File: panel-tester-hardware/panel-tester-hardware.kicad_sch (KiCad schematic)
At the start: 13 parts, among them J1 Screw_Terminal_01x02, J2 Conn_01x02, J3 Conn_01x07, Q1 BS170, U1 INA219AxD

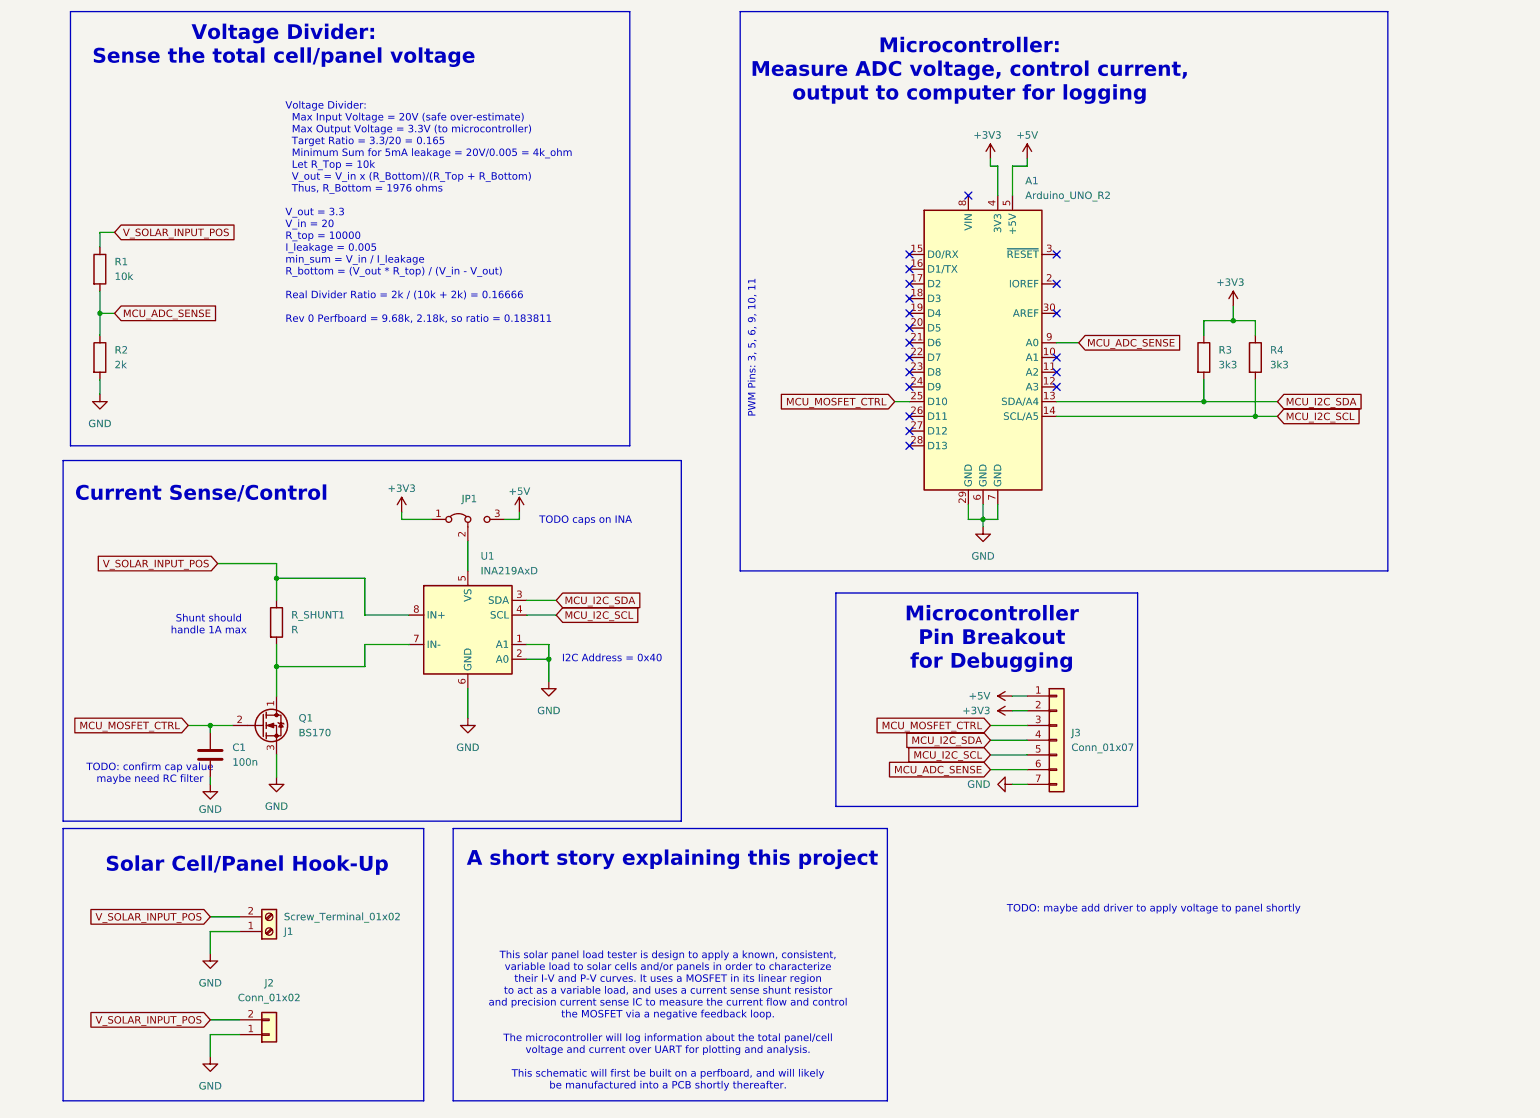
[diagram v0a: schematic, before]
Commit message: Changed Schematic Files
Modified Load Testing Schematic to use two current sensing mechanisms - (1) is the existing current sensing IC, MOSFET and shunt resistor and (2) is the new op-amp mechanism with the MOSFET and shunt resistor
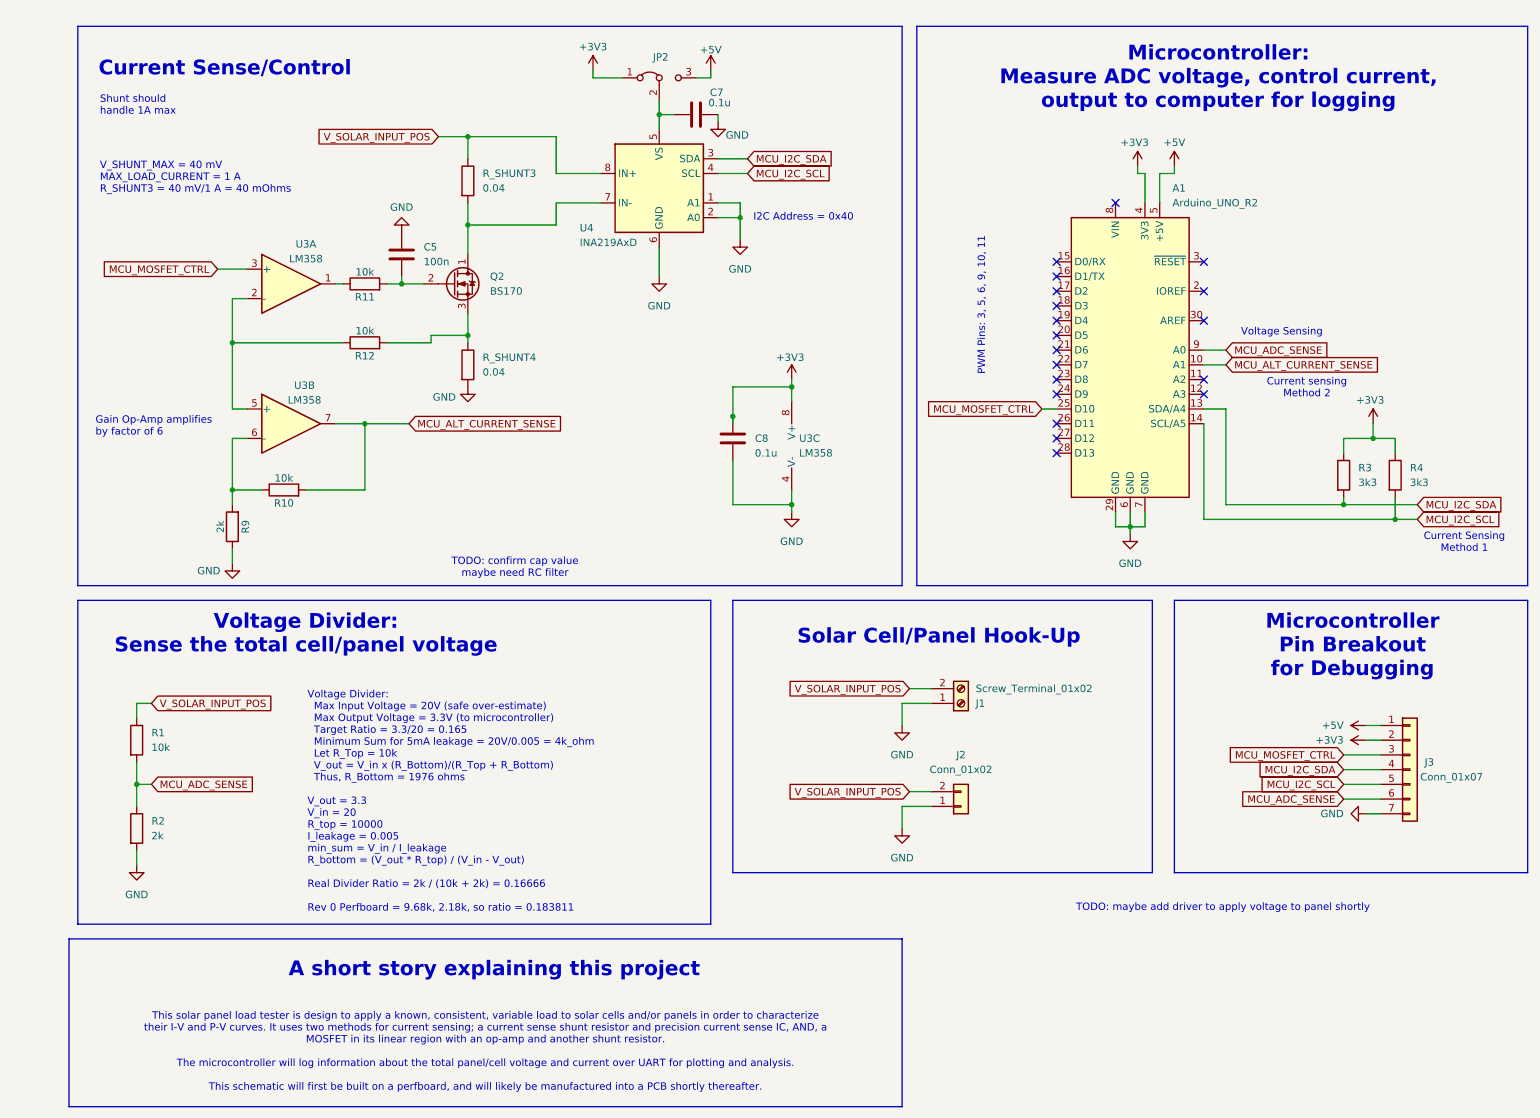
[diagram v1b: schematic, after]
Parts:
- removed C1: 100n, symbol Device:C
- removed JP1: Jumper_3_Bridged12, symbol Jumper:Jumper_3_Bridged12
- removed Q1: BS170, Package_TO_SOT_THT:TO-92_Inline, symbol Transistor_FET:BS170
- removed R_SHUNT1: R, symbol Device:R
- removed U1: INA219AxD, Package_SO:SOIC-8_3.9x4.9mm_P1.27mm, symbol Sensor_Energy:INA219AxD
- added C5: 100n, Capacitor_SMD:C_1206_3216Metric_Pad1.33x1.80mm_HandSolder, symbol Device:C
- added C7, C8: 0.1u, Capacitor_SMD:C_1206_3216Metric_Pad1.33x1.80mm_HandSolder, symbol Device:C
- added JP2: Jumper_3_Bridged12, Jumper:SolderJumper-3_P1.3mm_Open_RoundedPad1.0x1.5mm_NumberLabels, symbol Jumper:Jumper_3_Bridged12
- added Q2: BS170, Package_TO_SOT_THT:TO-92_Inline, symbol Transistor_FET:BS170
- added R10, R11, R12: 10k, Resistor_SMD:R_1206_3216Metric_Pad1.30x1.75mm_HandSolder, symbol Device:R
- added R9: 2k, Resistor_SMD:R_1206_3216Metric_Pad1.30x1.75mm_HandSolder, symbol Device:R
- added R_SHUNT3, R_SHUNT4: 0.04, Resistor_SMD:R_2512_6332Metric_Pad1.40x3.35mm_HandSolder, symbol Device:R
- added U3: LM358, Package_SO:SOIC-8_3.9x4.9mm_P1.27mm, symbol Amplifier_Operational:LM358
- added U4: INA219AxD, Package_SO:SOIC-8_3.9x4.9mm_P1.27mm, symbol Sensor_Energy:INA219AxD
- J1: footprint (none) -> TerminalBlock:TerminalBlock_bornier-2_P5.08mm
- J2: footprint (none) -> Connector_PinHeader_2.54mm:PinHeader_1x02_P2.54mm_Vertical
- J3: footprint (none) -> Connector_PinHeader_2.54mm:PinHeader_1x07_P2.54mm_Vertical
- R1, R2, R3, R4: footprint (none) -> Resistor_SMD:R_1206_3216Metric_Pad1.30x1.75mm_HandSolder
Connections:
- net +3V3: now also C8.1, JP2.1 (A), U3.8 (V+)
- net +5V: now also JP2.3 (B)
- net GND: now also C5.1, C7.2, C8.2, R9.1, R_SHUNT4.2, U3.4 (V-), U4.1 (A1), U4.2 (A0), U4.6 (GND)
- net MCU_I2C_SCL: now also U4.4 (SCL)
- net MCU_I2C_SDA: now also U4.3 (SDA)
- net MCU_MOSFET_CTRL: now also U3.3 (+)
- net V_SOLAR_INPUT_POS: now also R_SHUNT3.1, U4.8 (IN+)
- net MCU_ALT_CURRENT_SENSE: now reaches A1.10 (A1)
- net MCU_ALT_CURRENT_SENSE: now also R10.2, U3.7
- new net: R11.1, U3.1
- new net: R12.1, U3.2 (-), U3.5 (+)
- new net: C7.1, JP2.2 (C), U4.5 (VS)
- new net: C5.2, Q2.2 (G), R11.2
- new net: Q2.1 (D), R_SHUNT3.2, U4.7 (IN-)
- new net: Q2.3 (S), R12.2, R_SHUNT4.1
- new net: R10.1, R9.2, U3.6 (-)
- no-connect marks 20 -> 19
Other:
- note added: "Current Sensing Method 1"
- note added: "Current sensing Method 2"
- note added: "Gain Op-Amp amplifies by factor of 6"
- note added: "This solar panel load tester is design to apply a known, consistent, variable load to solar cells and/or panels in order to characterize their I-V and P-V curves. It uses two methods for current sensing; a current sense shunt resistor and precision current sense IC, AND, a MOSFET in its linear region with an op-amp and another shunt resistor. The microcontroller will log information about the tot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"
- note added: "V_SHUNT_MAX = 40 mV MAX_LOAD_CURRENT = 1 A R_SHUNT3 = 40 mV/1 A = 40 mOhms"
- note added: "Voltage Sensing"
- note removed: "TODO caps on INA"
- note removed: "This solar panel load tester is design to apply a known, consistent, variable load to solar cells and/or panels in order to characterize their I-V and P-V curves. It uses a MOSFET in its linear region to act as a variable load, and uses a current sense shunt resistor and precision current sense IC to measure the current flow and control the MOSFET via a negative feedback loop. The microcontroller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"
- moved on the sheet: A1, J1, J2, J3, R1, R2, R3, R4

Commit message: Did a lot of things
Created board layout and completed routing
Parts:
- Q2: footprint Package_TO_SOT_THT:TO-92_Inline -> Package_TO_SOT_THT:TO-220-3_Vertical
- U3: footprint Package_SO:SOIC-8_3.9x4.9mm_P1.27mm -> Package_DIP:DIP-8_W7.62mm_LongPads
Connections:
- net +3V3: now also J3.1 (Pin_1); no longer J3.2 (Pin_2)
- net +5V: now also J3.2 (Pin_2); no longer J3.1 (Pin_1)
- net MCU_ADC_SENSE: now also A1.10 (A1), J3.3 (Pin_3); no longer A1.9 (A0), J3.6 (Pin_6)
- net MCU_ALT_CURRENT_SENSE: now also A1.9 (A0); no longer A1.10 (A1)
- net MCU_I2C_SCL: now also J3.4 (Pin_4); no longer J3.5 (Pin_5)
- net MCU_I2C_SDA: now also J3.5 (Pin_5); no longer J3.4 (Pin_4)
- net MCU_MOSFET_CTRL: now also J3.6 (Pin_6); no longer J3.3 (Pin_3)

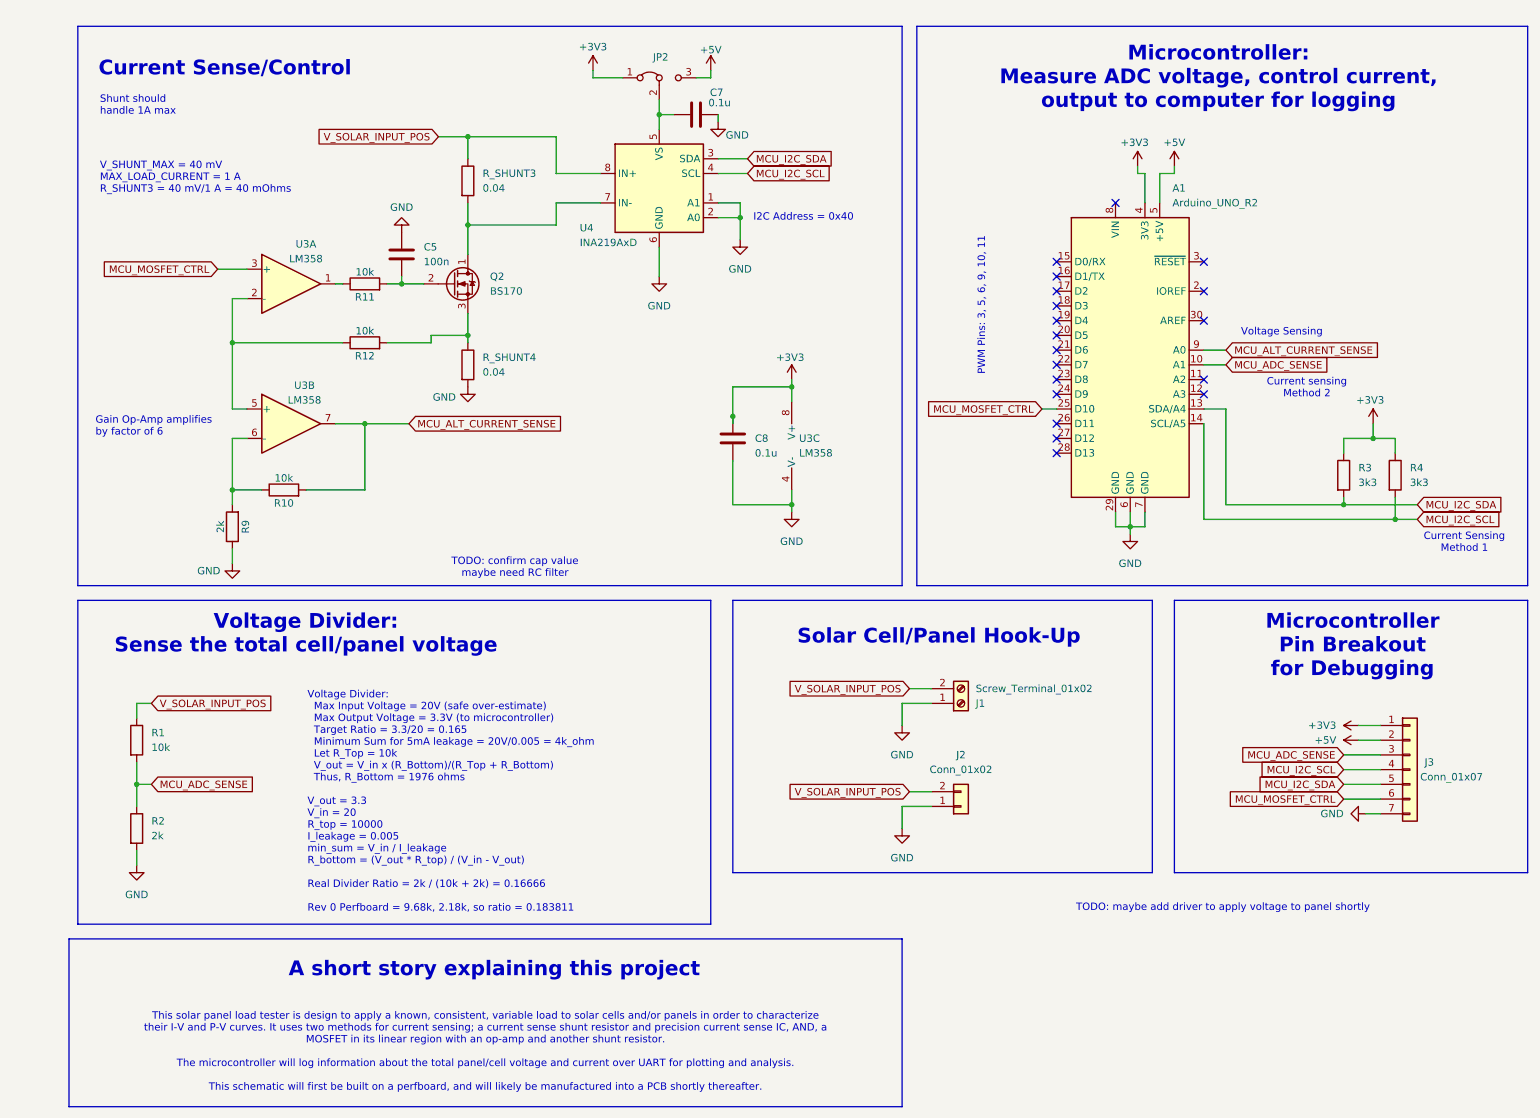
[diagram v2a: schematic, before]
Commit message: Updated schematic with DAC
Added MCP4921 for analog signal creation from Arduino PWM into the input of the Op-Amp.
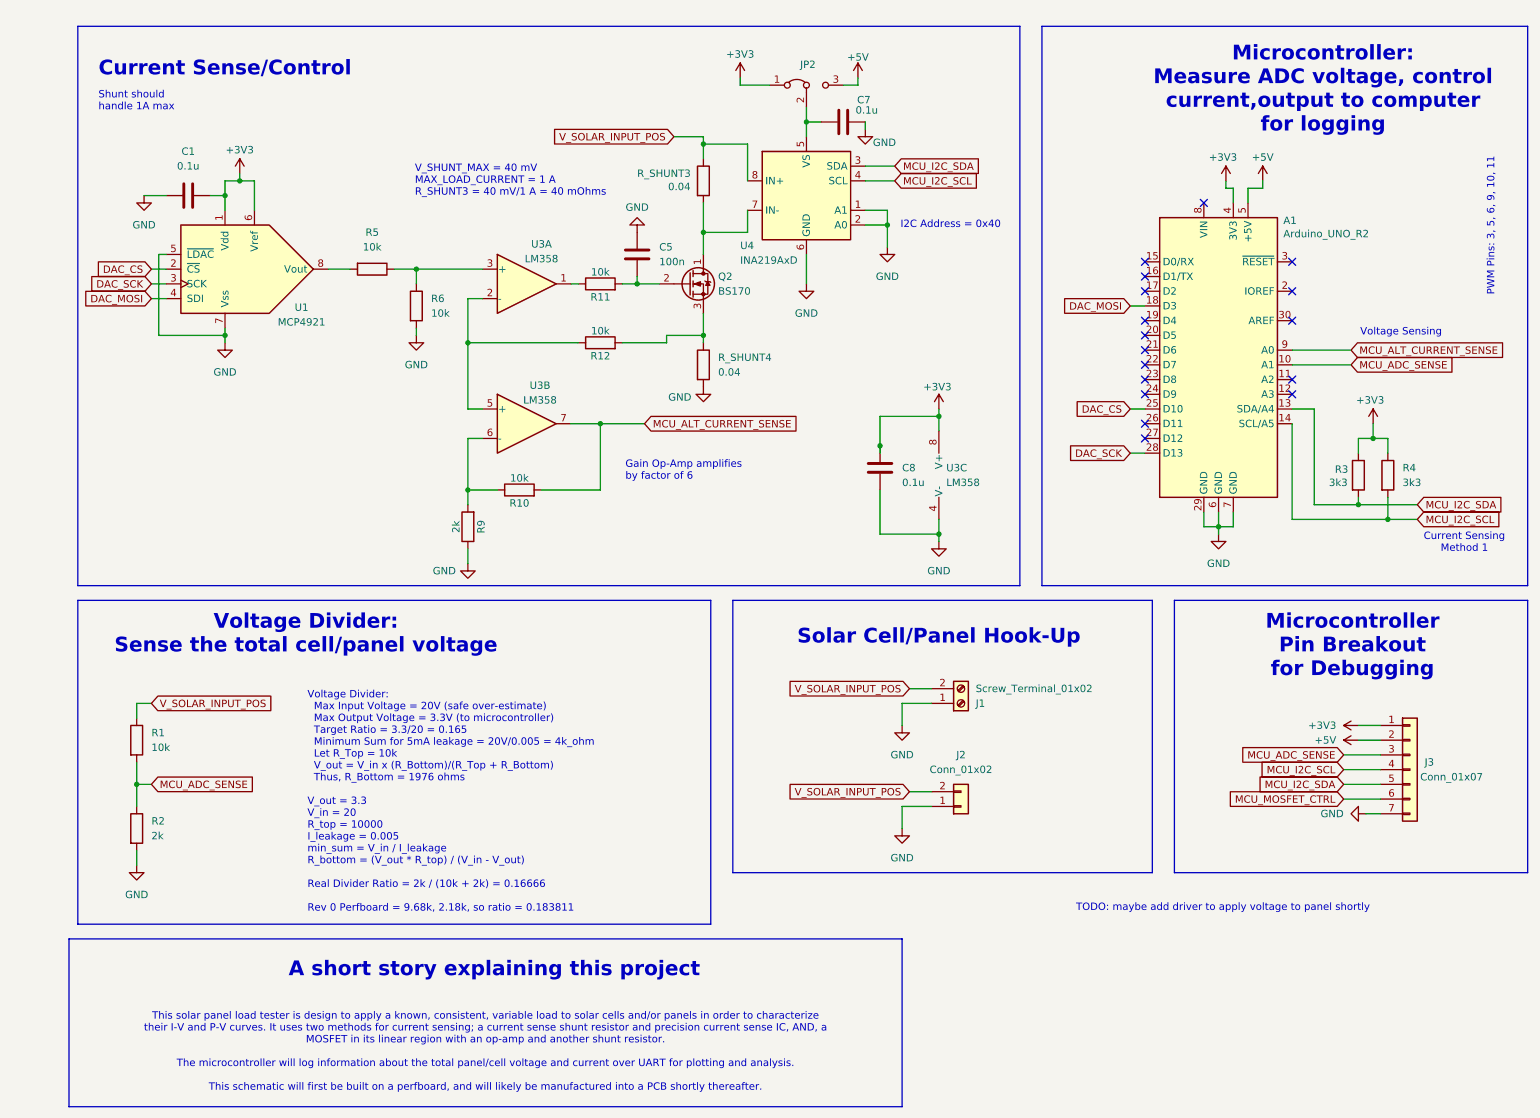
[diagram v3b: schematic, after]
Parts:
- added C1: 0.1u, Capacitor_SMD:C_1206_3216Metric_Pad1.33x1.80mm_HandSolder, symbol Device:C
- added R5, R6: 10k, Resistor_SMD:R_1206_3216Metric_Pad1.30x1.75mm_HandSolder, symbol Device:R
- added U1: MCP4921, symbol Analog_DAC:MCP4921
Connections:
- net +3V3: now also C1.2, U1.1 (Vdd), U1.6 (Vref)
- net GND: now also C1.1, R6.2, U1.5 (~{LDAC}), U1.7 (Vss)
- net MCU_MOSFET_CTRL: no longer A1.25 (D10), U3.3 (+)
- net DAC_MOSI: now reaches A1.18 (D3)
- net DAC_MOSI: now also U1.4 (SDI)
- net DAC_SCK: now reaches A1.28 (D13)
- net DAC_SCK: now also U1.3 (SCK)
- new net: R5.1, R6.1, U3.3 (+)
- new net: R5.2, U1.8 (Vout)
- new net DAC_CS: A1.25 (D10), U1.2 (~{CS})
- no-connect marks 19 -> 17
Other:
- note added: "Microcontroller: Measure ADC voltage, control current,output to computer for logging"
- note removed: "Current sensing Method 2"
- note removed: "Microcontroller: Measure ADC voltage, control current, output to computer for logging"
- note removed: "TODO: confirm cap value maybe need RC filter"
- moved on the sheet: A1, C5, C7, C8, JP2, Q2, R10, R11, R12, R3, R4, R9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

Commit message: Assigned footprints for DAC and additional passives
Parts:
- U1: footprint (none) -> Package_SO:SOIC-8_3.9x4.9mm_P1.27mm
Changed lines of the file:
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@@
 			)
 		)
-		(property "Footprint" ""
+		(property "Footprint" "Package_SO:SOIC-8_3.9x4.9mm_P1.27mm"
 			(at 66.04 59.69 0)
 			(effects

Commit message: Completed routing and aesthetic fixes
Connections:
- net MCU_MOSFET_CTRL is gone; now on net DAC_OUTPUT: J3.6 (Pin_6)
- net DAC_OUTPUT: now reaches R5.2, U1.8 (Vout)
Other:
- note added: "Optional Voltage Divider; R5 and R6 not needed"
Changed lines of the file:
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@@
+	)
+	(junction
+		(at 60.96 57.15)
+		(diameter 0)
+		(color 0 0 0 0)
 	)
 	(junction
@@
 	(wire
 		(pts
+			(xy 60.96 57.15) (xy 62.23 57.15)
+		)
+		(stroke
+			(width 0)
+			(type default)
+		)
+	)
+	(wire
+		(pts
 			(xy 130.81 41.91) (xy 130.81 35.56)
 		)
@@
 	(wire
 		(pts
+			(xy 60.96 50.8) (xy 60.96 57.15)
+		)
+		(stroke
+			(width 0)
+			(type default)
+		)
+	)
+	(wire
+		(pts
 			(xy 162.56 149.86) (xy 157.48 149.86)
 		)
@@
 	(wire
 		(pts
-			(xy 58.42 57.15) (xy 62.23 57.15)
+			(xy 58.42 57.15) (xy 60.96 57.15)
 		)
 		(stroke
@@
 		(fill
 			(type none)
+		)
+	)
+	(text "Optional Voltage Divider;\nR5 and R6 not needed"
+		(exclude_from_sim no)
+		(at 66.294 79.502 0)
+		(effects
+			(font
+				(size 1.27 1.27)
+			)
 		)
 	)
@@
 		)
 	)
-	(global_label "MCU_MOSFET_CTRL"
+	(global_label "DAC_OUTPUT"
 		(shape input)
 		(at 233.68 148.59 180)
@@
 		)
 		(property "Intersheetrefs" "${INTERSHEET_REFS}"
-			(at 212.9754 148.59 0)
+			(at 218.9019 148.59 0)
 			(effects
 				(font
@@
 				(hide yes)
 			)
+		)
+	)
+	(global_label "DAC_OUTPUT"
+		(shape input)
+		(at 60.96 50.8 90)
+		(fields_autoplaced yes)
+		(effects
+			(font
+				(size 1.27 1.27)
+			)
+			(justify left)
+		)
+		(property "Intersheetrefs" "${INTERSHEET_REFS}"
+			(at 60.96 36.0219 90)
+			(effects
+				(font
+					(size 1.27 1.27)
+				)
+				(justify left)
+				(hide yes)
+			)

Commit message: Revert "Bluepill layout edits"
This reverts commit 7404dadbf005f9dc7929b7ea0254307db19fd9e4.
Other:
- note added: "Microcontroller: Measure ADC voltage, control current, log to computer"
- note removed: "Microcontroller: Measure ADC voltage, control current,output to computer for logging"
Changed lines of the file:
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@@
 	(generator_version "8.0")
 	(paper "USLetter")
-	(title_block
-		(date "2024-03-15")
-		(rev "Rev 0")
-	)
 	(junction
 		(at 105.41 83.82)
@@
 		)
 	)
-	(text "Microcontroller:\nMeasure ADC voltage, control \ncurrent,output to computer \nfor logging"
+	(text "Microcontroller:\nMeasure ADC voltage, control \ncurrent, log to computer "
 		(exclude_from_sim no)
 		(at 230.124 26.162 0)

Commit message: Bluepill layout edits
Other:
- note added: "Microcontroller: Measure ADC voltage, control current,output to computer for logging"
- note removed: "Microcontroller: Measure ADC voltage, control current, log to computer"
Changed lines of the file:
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@@
 	(generator_version "8.0")
 	(paper "USLetter")
+	(title_block
+		(date "2024-03-15")
+		(rev "Rev 0")
+	)
 	(junction
 		(at 105.41 83.82)
@@
 		)
 	)
-	(text "Microcontroller:\nMeasure ADC voltage, control \ncurrent, log to computer "
+	(text "Microcontroller:\nMeasure ADC voltage, control \ncurrent,output to computer \nfor logging"
 		(exclude_from_sim no)
 		(at 230.124 26.162 0)
